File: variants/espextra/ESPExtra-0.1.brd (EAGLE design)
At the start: 95.6 x 57.1 mm, 15 parts, among them U1 ESP12E_DEVKIT, U2 MCP23S17SP, U3 MCP23S17SP, U4 MCP3008

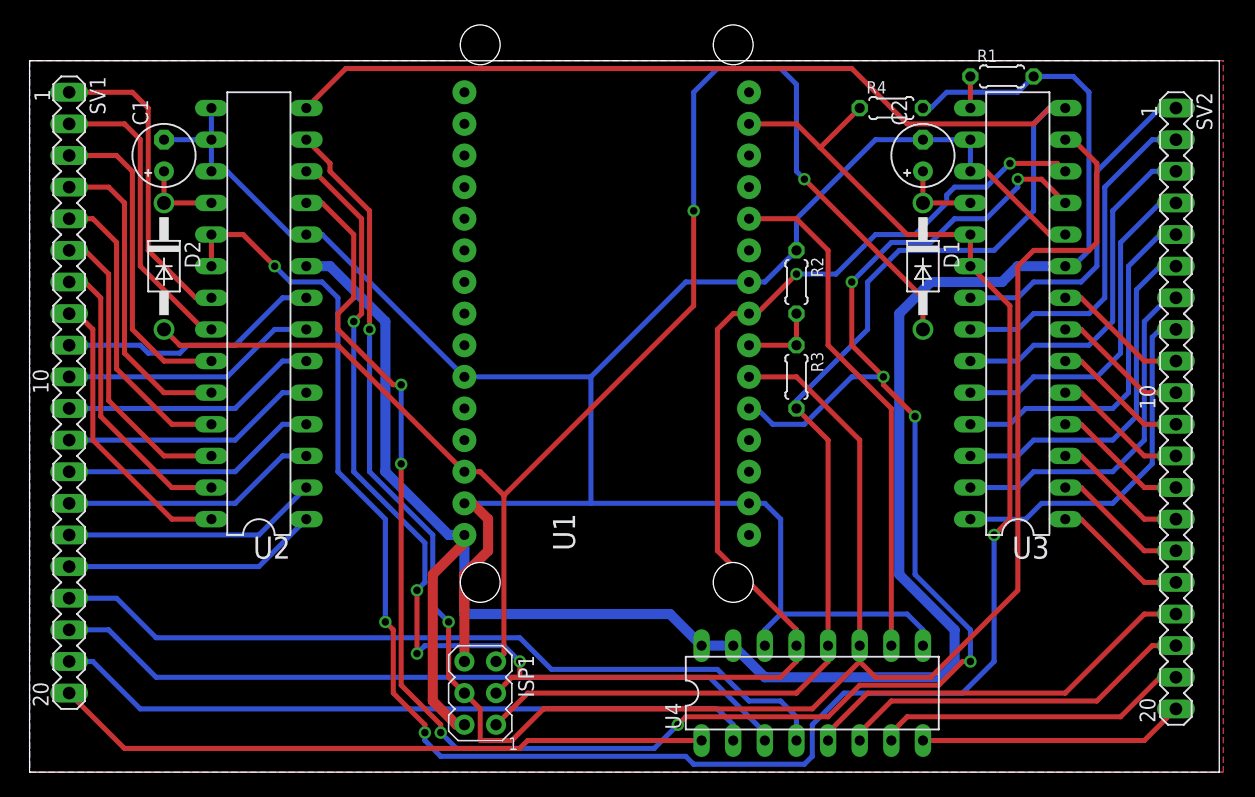
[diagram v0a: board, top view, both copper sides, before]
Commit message: Previous commit failed to update board files
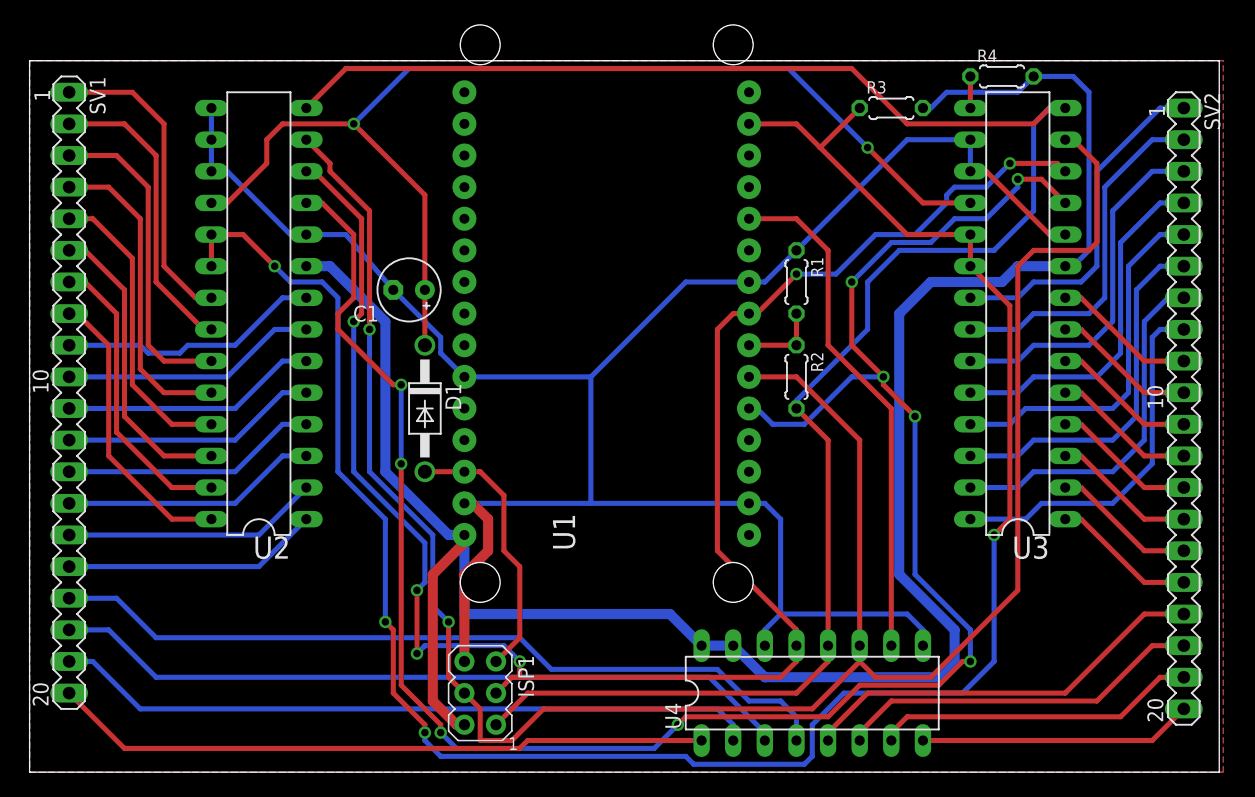
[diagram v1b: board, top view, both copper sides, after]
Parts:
- removed C2: 10u, resistor:E2,5-5
- removed D2: 1N4004, diode:DO41-10
- R1: value 4k7 -> 910
- R2: value 910 -> 470
- R3: value 470 -> 4k7
- moved D1 41.6 mm to (31.8, 29.2)
- moved R1 23.3 mm to (61.6, 39.4), turned to 270 degrees
- moved R3 22.9 mm to (69.2, 53.3), turned to 0 degrees
- moved C1 22.5 mm to (30.5, 38.7), turned to 180 degrees
- moved R4 9.25 mm to (78.1, 55.9)
- moved R2 7.62 mm to (61.6, 31.8)
- moved SV2 0.63 mm to (92.7, 29.2)
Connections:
- removed net N$3: C2.+, D1.C, U3.18
- removed net N$30: C1.+, D2.C, U2.18
- new net RST_D: C1.+, D1.C, U2.18, U3.18
- net +5V: now also R3.2; no longer R1.2
- net GND: now also R1.1; no longer C2.-, R2.1
- net INT: now also R3.1; no longer R4.1
- net MISO: now also R2.2; no longer R3.2
- net N$11: now also R1.2, R2.1; no longer R2.2, R3.1
- net N$25: now also R4.1; no longer R1.1
- net RST: no longer D2.A
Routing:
- net RST: track 118.6 -> 21.8 mm, vias 2 -> 0
- net RST_D: track 0.00 -> 91.2 mm, vias 0 -> 2
- net N$3: track 6.35 -> 0.00 mm
- net N$30: track 6.35 -> 0.00 mm
- net GND: track 173.0 -> 168.6 mm
- net A8: track 21.4 -> 22.0 mm
- net D31: track 11.0 -> 11.6 mm
- net D30: track 11.0 -> 11.6 mm
- net D29: track 11.0 -> 11.6 mm
- net D28: track 11.0 -> 11.6 mm
- net D27: track 11.0 -> 11.6 mm
- net D26: track 11.0 -> 11.6 mm
- net D25: track 11.0 -> 11.6 mm
- net D24: track 11.0 -> 11.6 mm
- net D23: track 28.8 -> 29.4 mm
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
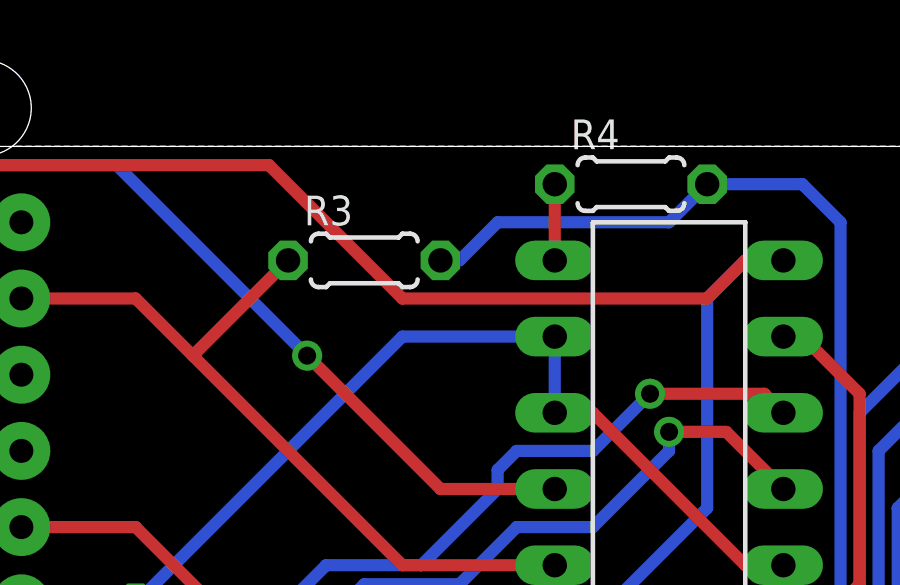
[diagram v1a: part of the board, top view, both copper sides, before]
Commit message: Resistor removed, internal pullup is used for interrupt pin. Also, before SPI transactions, set the appropriate SPI settings, just to be sure.
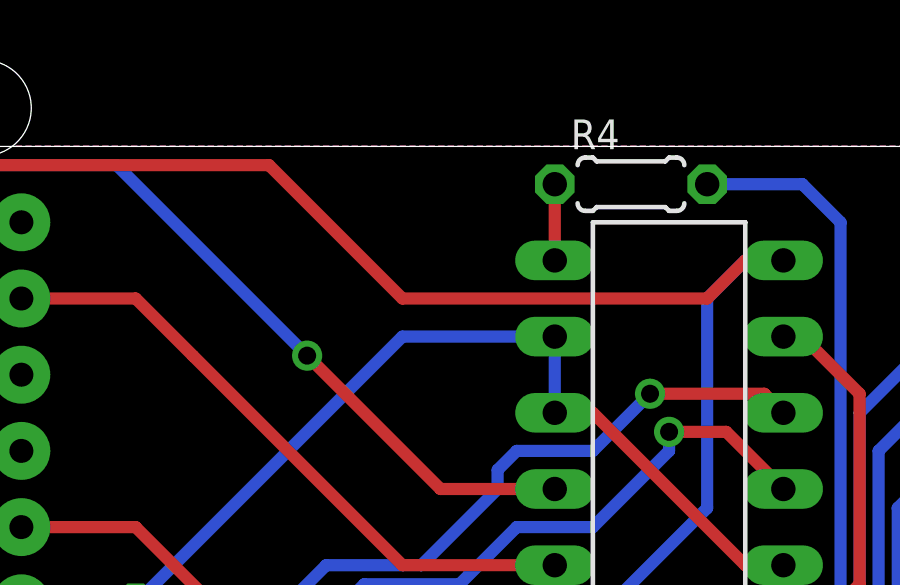
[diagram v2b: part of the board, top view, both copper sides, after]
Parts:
- removed R3: 4k7, resistor:0204/5
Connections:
- net +5V: no longer R3.2
- net INT: no longer R3.1
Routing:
- net +5V: track 170.2 -> 160.2 mm
- net INT: track 166.8 -> 162.3 mm
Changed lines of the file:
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@@
 </element>
 <element name="U4" library="adafruit" package="DIL16" value="MCP3008" x="62.865" y="6.35"/>
-<element name="R3" library="resistor" package="0204/5" value="4k7" x="69.215" y="53.34"/>
 </elements>
 <signals>
@@
 <via x="31.75" y="3.175" extent="1-16" drill="0.6"/>
 <via x="77.47" y="19.05" extent="1-16" drill="0.6"/>
-<contactref element="R3" pad="1"/>
-<wire x1="66.675" y1="53.34" x2="63.5" y2="50.165" width="0.4064" layer="1"/>
 </signal>
 <signal name="D16">
@@
 <wire x1="32.385" y1="15.875" x2="34.925" y2="18.415" width="0.8128" layer="1"/>
 <wire x1="34.925" y1="18.415" x2="34.925" y2="19.05" width="0.8128" layer="1"/>
-<contactref element="R3" pad="2"/>
-<wire x1="71.755" y1="53.34" x2="72.39" y2="53.34" width="0.4064" layer="16"/>
-<wire x1="72.39" y1="53.34" x2="73.66" y2="54.61" width="0.4064" layer="16"/>
-<wire x1="73.66" y1="54.61" x2="79.375" y2="54.61" width="0.4064" layer="16"/>
-<wire x1="79.375" y1="54.61" x2="80.645" y2="55.88" width="0.4064" layer="16"/>
 </signal>
 <signal name="A1">
